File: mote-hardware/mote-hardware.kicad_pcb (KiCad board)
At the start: 2 copper layers, 52 x 51 mm, 43 parts, among them J1 USB_B_Micro, J2 Conn_02x18_Odd_Even, J3 Conn_02x18_Odd_Even, J4 SM03B-SRSS-TB, SW1 SW_Push, SW2 SW_Push, U1 RP2350_60QFN, U2 NCP1117-3.3_SOT223, U3 W25Q128JVS, Y1 ABM8-272-T3

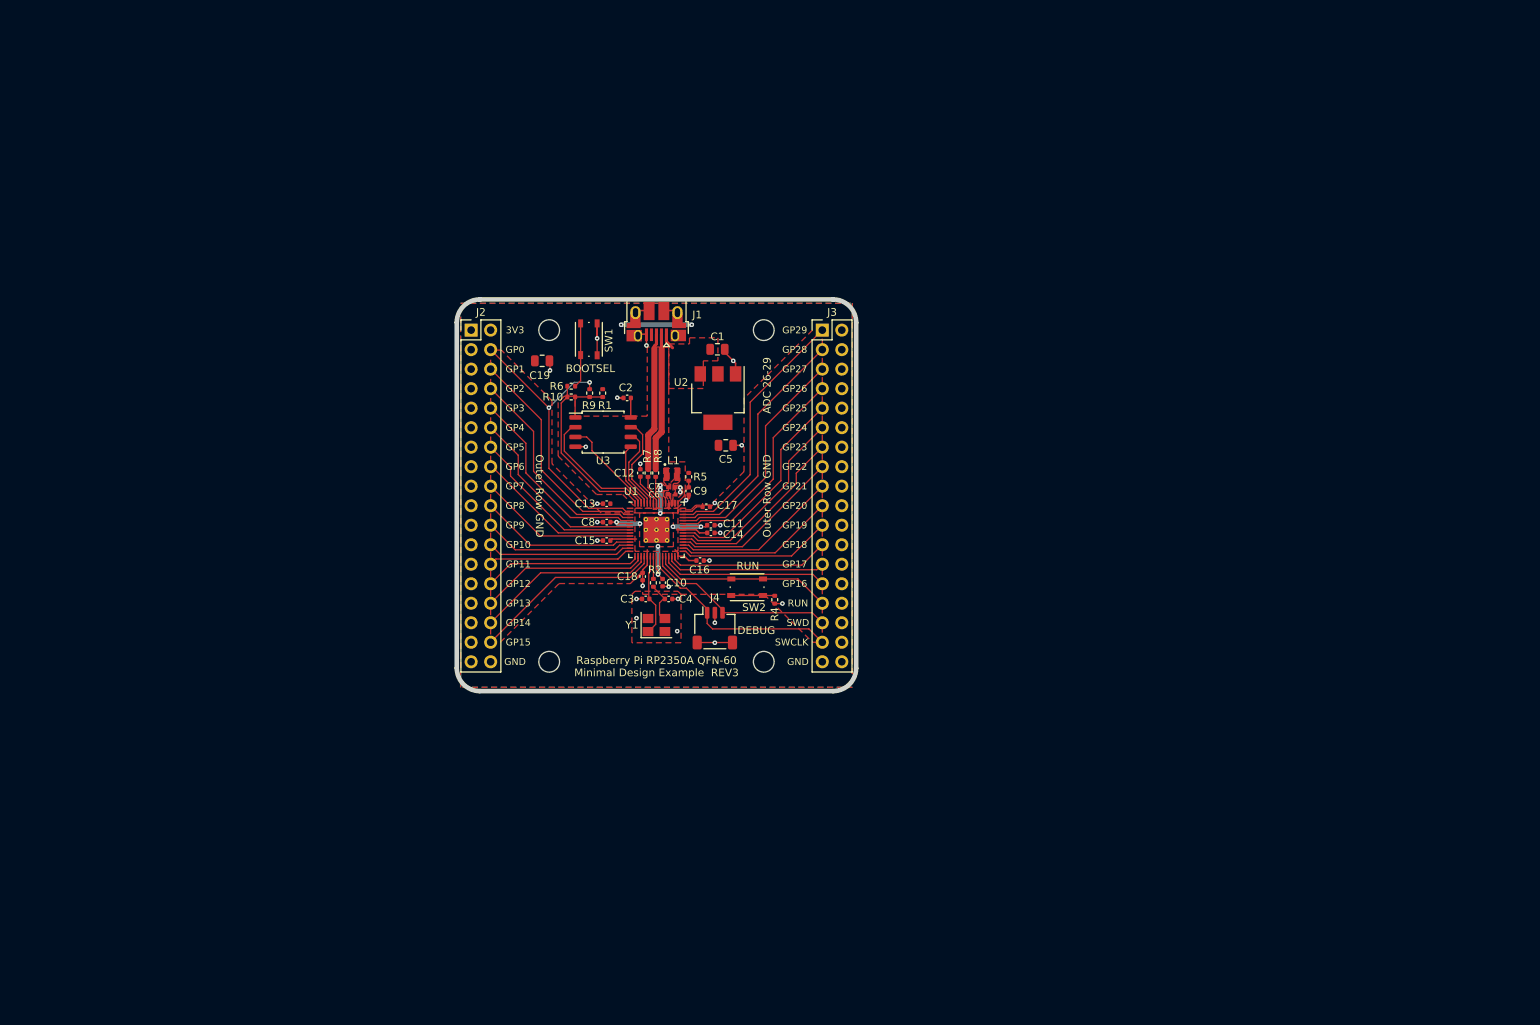
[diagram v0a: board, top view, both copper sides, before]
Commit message: Start of PCB layout
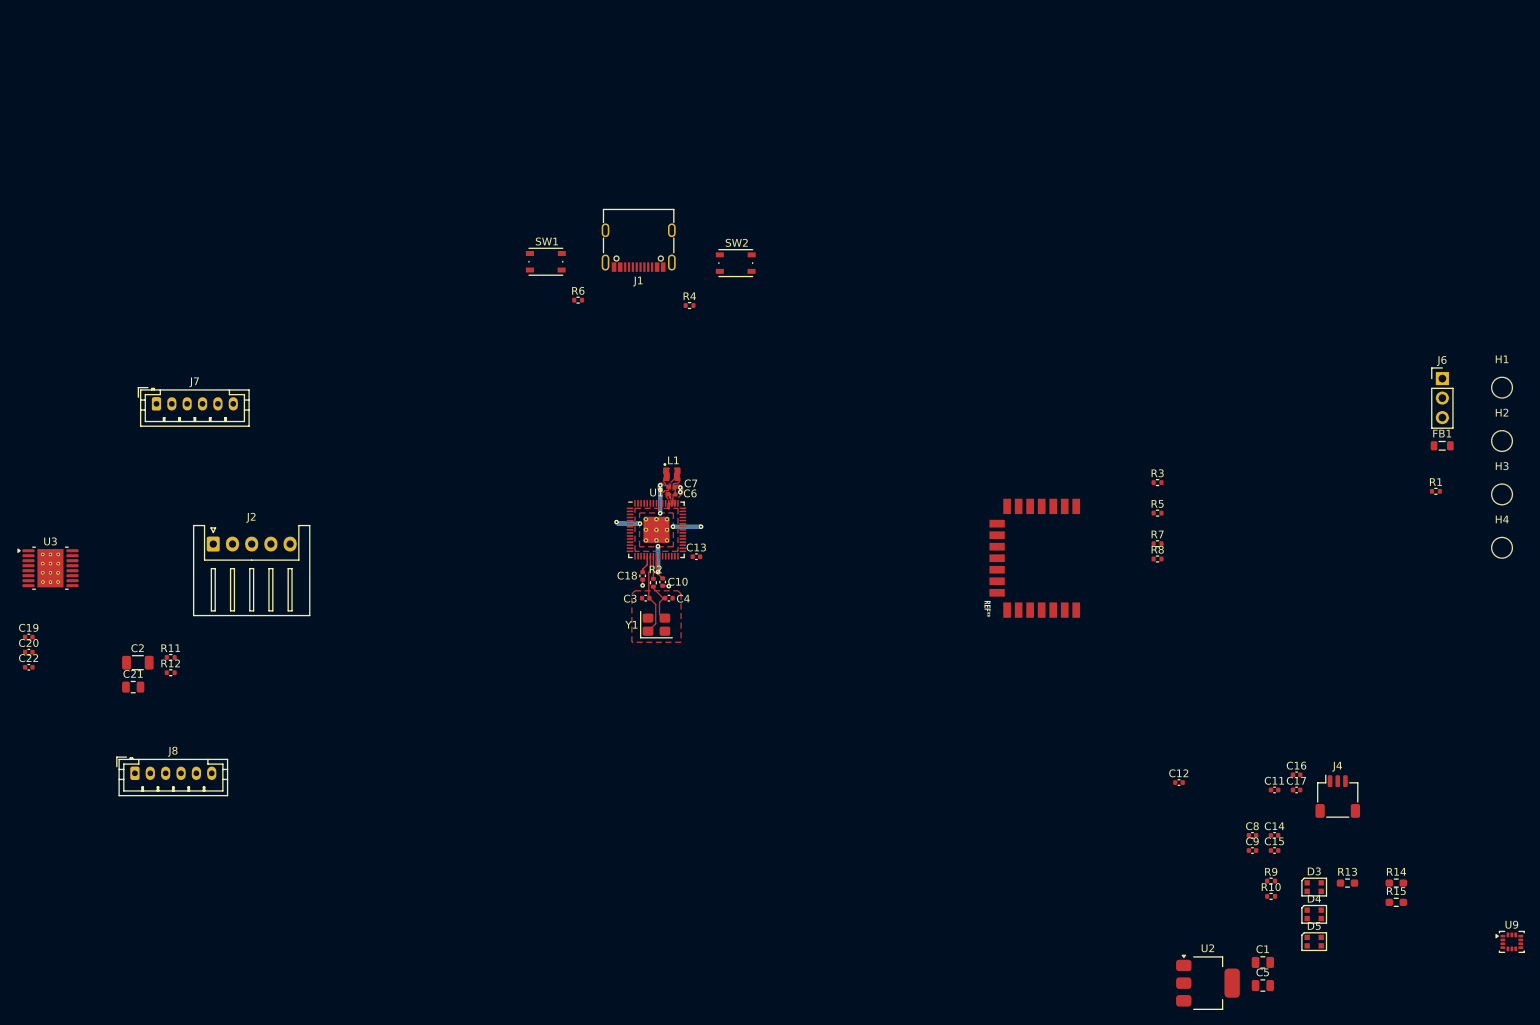
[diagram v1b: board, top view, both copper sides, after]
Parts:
- removed J3: Conn_02x18_Odd_Even, Connector_PinHeader_2.54mm:PinHeader_2x18_P2.54mm_Vertical
- added C20: 2.2u, Capacitor_SMD:C_0402_1005Metric, F.Cu at (18.3, 115.9)
- added C21: 10uF, Capacitor_SMD:C_0805_2012Metric, F.Cu at (31.9, 120.5)
- added C22: 0.1uF, Capacitor_SMD:C_0402_1005Metric, F.Cu at (18.3, 117.9)
- added D3: WS2812B-2020, LED_SMD:LED_WS2812B-2020_PLCC4_2.0x2.0mm, F.Cu at (185.6, 146.5)
- added D4: WS2812B-2020, LED_SMD:LED_WS2812B-2020_PLCC4_2.0x2.0mm, F.Cu at (185.6, 150.1)
- added D5: WS2812B-2020, LED_SMD:LED_WS2812B-2020_PLCC4_2.0x2.0mm, F.Cu at (185.6, 153.6)
- added FB1: 300, Inductor_SMD:L_0805_2012Metric, F.Cu at (202.3, 89.1)
- added J6: Conn_01x03_Pin, Connector_PinHeader_2.54mm:PinHeader_1x03_P2.54mm_Vertical, F.Cu at (202.3, 80.3)
- added J7: left_motor, Connector_JST:JST_PH_B6B-PH-K_1x06_P2.00mm_Vertical, F.Cu at (34.9, 83.6)
- added J8: right_motor, Connector_JST:JST_PH_B6B-PH-K_1x06_P2.00mm_Vertical, F.Cu at (32.1, 131.7)
- added R11: 200m, Resistor_SMD:R_0402_1005Metric, F.Cu at (36.8, 116.6)
- added R12: 200m, Resistor_SMD:R_0402_1005Metric, F.Cu at (36.8, 118.6)
- added R13: 560, Resistor_SMD:R_0603_1608Metric_Pad0.98x0.95mm_HandSolder, F.Cu at (190.0, 146.0)
- added R14: 10k, Resistor_SMD:R_0603_1608Metric_Pad0.98x0.95mm_HandSolder, F.Cu at (196.3, 146.0)
- added R15: 10k, Resistor_SMD:R_0603_1608Metric_Pad0.98x0.95mm_HandSolder, F.Cu at (196.3, 148.5)
- added R3: 10k, Resistor_SMD:R_0402_1005Metric, F.Cu at (165.2, 93.8)
- added U4: RP Radio Module 2, mote-hardware:rpi_rmc20452t, F.Cu at (152.1, 103.7)
- added U9: LSM6DS3, Package_LGA:LGA-14_3x2.5mm_P0.5mm_LayoutBorder3x4y, F.Cu at (211.4, 153.7)
- C19: value 10u -> 0.01u; footprint Capacitor_SMD:C_0805_2012Metric -> Capacitor_SMD:C_0402_1005Metric
- C2: value 100n -> 100uF; footprint Capacitor_SMD:C_0402_1005Metric -> Capacitor_SMD:C_1206_3216Metric
- H1, H2, H3, H4: value MountingHole -> M2.5 loose
- J1: value USB_B_Micro -> USB_C_Receptacle_USB2.0_14P; footprint Connector_USB:USB_Micro-B_Amphenol_10103594-0001LF_Horizontal -> Connector_USB:USB_C_Receptacle_G-Switch_GT-USB-7010ASV
- J2: value Conn_02x18_Odd_Even -> JST_XH2.54-SP; footprint Connector_PinHeader_2.54mm:PinHeader_2x18_P2.54mm_Vertical -> Connector_JST:JST_XH_S5B-XH-A_1x05_P2.50mm_Horizontal
- R1: value DNF -> 470
- R10: value 0 -> 5.1k
- R9: value DNF -> 5.1k
- U3: value W25Q128JVS -> DRV8833PWP; footprint Package_SO:SOIC-8_5.23x5.23mm_P1.27mm -> Package_SO:HTSSOP-16-1EP_4.4x5mm_P0.65mm_EP3.4x5mm_Mask2.46x2.31mm_ThermalVias
- moved H4 124.9 mm to (210.1, 102.3)
- moved H1 124.3 mm to (210.1, 81.5)
- moved R10 111.9 mm to (180.0, 147.7)
- moved R1 109.2 mm to (201.5, 95.0), turned to 0 degrees
- moved R9 109.1 mm to (180.0, 145.7), turned to 0 degrees
- moved C1 106.8 mm to (178.9, 156.3)
- moved U2 99.4 mm to (171.8, 159.0), turned to 0 degrees
- moved C5 99.2 mm to (178.9, 159.3)
- moved H3 98.6 mm to (210.1, 95.4)
- moved H2 97.2 mm to (210.1, 88.4)
- moved C15 95.9 mm to (180.5, 141.8), turned to 0 degrees
- moved C8 93.4 mm to (177.6, 139.8), turned to 0 degrees
- moved C9 87.1 mm to (177.6, 141.8), turned to 0 degrees
- moved C17 85.2 mm to (183.3, 133.9)
- moved J4 84.0 mm to (188.7, 134.7)
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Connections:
- net +1V1 renamed /rp2354/+1v1
- net /RUN renamed /rp2354/RUN
- net /SWCLK renamed /rp2354/SWCLK
- net /SWD renamed /rp2354/SWD
- net /VREG_AVDD renamed /rp2354/VREG_AVDD
- net /VREG_LX renamed /rp2354/VREG_LX
- net /XIN renamed /rp2354/XIN
- net /XOUT renamed /rp2354/XOUT
- net /~{USB_BOOT} renamed /rp2354/~{USB_BOOT}
- C1 pad 1: VBUS -> /+5v
- C12 pad 1: +3V3 -> /+3v3
- C13 pad 1: +3V3 -> /+3v3
- C14 pad 1: +3V3 -> /+3v3
- C15 pad 1: +3V3 -> /+3v3
- C16 pad 1: +3V3 -> /+3v3
- C17 pad 1: +3V3 -> /+3v3
- C18 pad 1: +3V3 -> /+3v3
- C19 pad 1: +3V3 -> Net-(U3-VCP)
- C19 pad 2: GND -> /+5v
- C2 pad 1: +3V3 -> /+5v
- C5 pad 1: +3V3 -> /+3v3
- C6 pad 1: +3V3 -> /+3v3
- J2 pad 1: GND -> /+5v
- J2 pad 2: +3V3 -> /lidar_rx
- J2 pad 3: GND -> /lidar_tx
- J2 pad 4: /GPIO0 -> GND
- J2 pad 5: GND -> unconnected-(J2-Pin_5-Pad5)
- R1 pad 1: +3V3 -> /rp2354/GPIO24
- R1 pad 2: /FLASH_SS -> Net-(U4-DO)
- R10 pad 1: /QSPI_SS -> /CC2
- R10 pad 2: /FLASH_SS -> GND
- R5 pad 1: +3V3 -> /+3v3
- R6 pad 1: /QSPI_SS -> /rp2354/QSPI_SS
- R9 pad 1: /GPIO0 -> /CC1
- R9 pad 2: /FLASH_SS -> GND
- U1 pad 1: +3V3 -> /+3v3
- U1 pad 10: /GPIO7 -> /motor_left_encoder_b
- U1 pad 11: +3V3 -> /+3v3
- U1 pad 12: /GPIO8 -> /motor_right_encoder_a
- U1 pad 13: /GPIO9 -> /motor_right_encoder_b
- U1 pad 14: /GPIO10 -> /motor_left_input_a
- U1 pad 15: /GPIO11 -> /motor_left_input_b
- U1 pad 16: /GPIO12 -> /motor_right_input_a
- U1 pad 17: /GPIO13 -> /motor_right_input_b
- U1 pad 18: /GPIO14 -> /imu_sda
- U1 pad 19: /GPIO15 -> /imu_scl
- U1 pad 2: /GPIO0 -> /rp2354/GPIO0
- U1 pad 20: +3V3 -> /+3v3
- U1 pad 27: /GPIO16 -> /rp2354/GPIO16
- U1 pad 28: /GPIO17 -> /rp2354/GPIO17
- U1 pad 29: /GPIO18 -> /motor_standby
- U1 pad 3: /GPIO1 -> /rp2354/GPIO1
- U1 pad 30: +3V3 -> /+3v3
- U1 pad 31: /GPIO19 -> /status_led_tx
- U1 pad 32: /GPIO20 -> /rp2354/GPIO20
- U1 pad 33: /GPIO21 -> /rp2354/GPIO21
- U1 pad 34: /GPIO22 -> /rp2354/GPIO22
- U1 pad 35: /GPIO23 -> /rp2354/GPIO23
- U1 pad 36: /GPIO24 -> /rp2354/GPIO24
- U1 pad 37: /GPIO25 -> /rp2354/GPIO25
- U1 pad 38: +3V3 -> /+3v3
- U1 pad 4: /GPIO2 -> /rp2354/GPIO2
- U1 pad 40: /GPIO26_ADC0 -> /CC1
- U1 pad 41: /GPIO27_ADC1 -> /CC2
- U1 pad 42: /GPIO28_ADC2 -> /rp2354/GPIO28_ADC2
- U1 pad 43: /GPIO29_ADC3 -> /rp2354/GPIO29_ADC3
- U1 pad 44: +3V3 -> /+3v3
- U1 pad 45: +3V3 -> /+3v3
- U1 pad 49: +3V3 -> /+3v3
- U1 pad 5: /GPIO3 -> /rp2354/GPIO3
- U1 pad 53: +3V3 -> /+3v3
- U1 pad 54: +3V3 -> /+3v3
- U1 pad 55: /QSPI_SD3 -> /rp2354/QSPI_SD3
- U1 pad 56: /QSPI_SCLK -> /rp2354/QSPI_SCLK
- U1 pad 57: /QSPI_SD0 -> /rp2354/QSPI_SD0
- U1 pad 58: /QSPI_SD2 -> /rp2354/QSPI_SD2
- U1 pad 59: /QSPI_SD1 -> /rp2354/QSPI_SD1
- U1 pad 60: /QSPI_SS -> /rp2354/QSPI_SS
- U1 pad 7: /GPIO4 -> /lidar_tx
- U1 pad 8: /GPIO5 -> /lidar_rx
- U1 pad 9: /GPIO6 -> /motor_left_encoder_a
- U2 pad 2: +3V3 -> /+3v3
- U2 pad 3: VBUS -> /+5v
- U3 pad 1: /FLASH_SS -> /motor_standby
- U3 pad 2: /QSPI_SD1 -> Net-(J7-Pin_5)
- U3 pad 3: /QSPI_SD2 -> Net-(U3-AISEN)
- U3 pad 4: GND -> Net-(J7-Pin_6)
- U3 pad 5: /QSPI_SD0 -> Net-(J8-Pin_6)
- U3 pad 6: /QSPI_SCLK -> Net-(U3-BISEN)
- U3 pad 7: /QSPI_SD3 -> Net-(J8-Pin_5)
- U3 pad 8: +3V3 -> unconnected-(U3-~{FAULT}-Pad8)
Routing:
- net /GPIO0: track 39.0 -> 0.00 mm, vias 2 -> 0
- net +3V3: track 37.6 -> 0.00 mm, vias 2 -> 0
- net GND: track 37.5 -> 1.58 mm, vias 27 -> 4
- net /GPIO29_ADC3: track 33.6 -> 0.00 mm
- net /GPIO28_ADC2: track 31.9 -> 0.00 mm
- net /GPIO27_ADC1: track 30.3 -> 0.00 mm
- net /GPIO1: track 29.8 -> 0.00 mm
- net /GPIO26_ADC0: track 28.6 -> 0.00 mm
- net /GPIO2: track 28.2 -> 0.00 mm
- net /rp2354/SWCLK: track 27.8 -> 0.00 mm
- net /GPIO25: track 27.7 -> 0.00 mm
- net /GPIO3: track 26.5 -> 0.00 mm
- net /GPIO24: track 26.1 -> 0.00 mm
- net /rp2354/SWD: track 25.4 -> 0.00 mm
- net /GPIO15: track 25.2 -> 0.00 mm
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- added copper zone on F.Cu, net +1V1
- added copper zone on F.Cu, net /VREG_LX
- removed copper zone on F.Cu, net /rp2354/+1v1
- removed copper zone on F.Cu, net /rp2354/VREG_LX
- removed copper zone on B.Cu, net GND
- removed copper zone on F.Cu, net VBUS
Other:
- board outline removed
- board text removed: "3V3"
- board text removed: "ADC 26-29"
- board text removed: "BOOTSEL"
- board text removed: "DEBUG"
- board text removed: "GND"
- board text removed: "GP0"
- board text removed: "GP1"
- board text removed: "GP10"
- board text removed: "GP11"
- board text removed: "GP12"
- board text removed: "GP13"
- board text removed: "GP14"
- board text removed: "GP15"
- board text removed: "GP16"
- board text removed: "GP17"
- board text removed: "GP18"
- board text removed: "GP19"
- board text removed: "GP2"
- board text removed: "GP20"
- board text removed: "GP21"
- board text removed: "GP22"
- board text removed: "GP23"
- board text removed: "GP24"
- board text removed: "GP25"
- board text removed: "GP26"
- board text removed: "GP27"
- board text removed: "GP28"
- board text removed: "GP29"
- board text removed: "GP3"
- board text removed: "GP4"
- board text removed: "GP5"
- board text removed: "GP6"
- board text removed: "GP7"
- board text removed: "GP8"
- board text removed: "GP9"
- board text removed: "Minimal Design Example REV3"
- board text removed: "Outer Row GND"
- board text removed: "RUN"
- board text removed: "Raspberry Pi RP2350A QFN-60"
- board text removed: "SWCLK"
- board text removed: "SWD"

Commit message: Get pcb ready for first prototype order
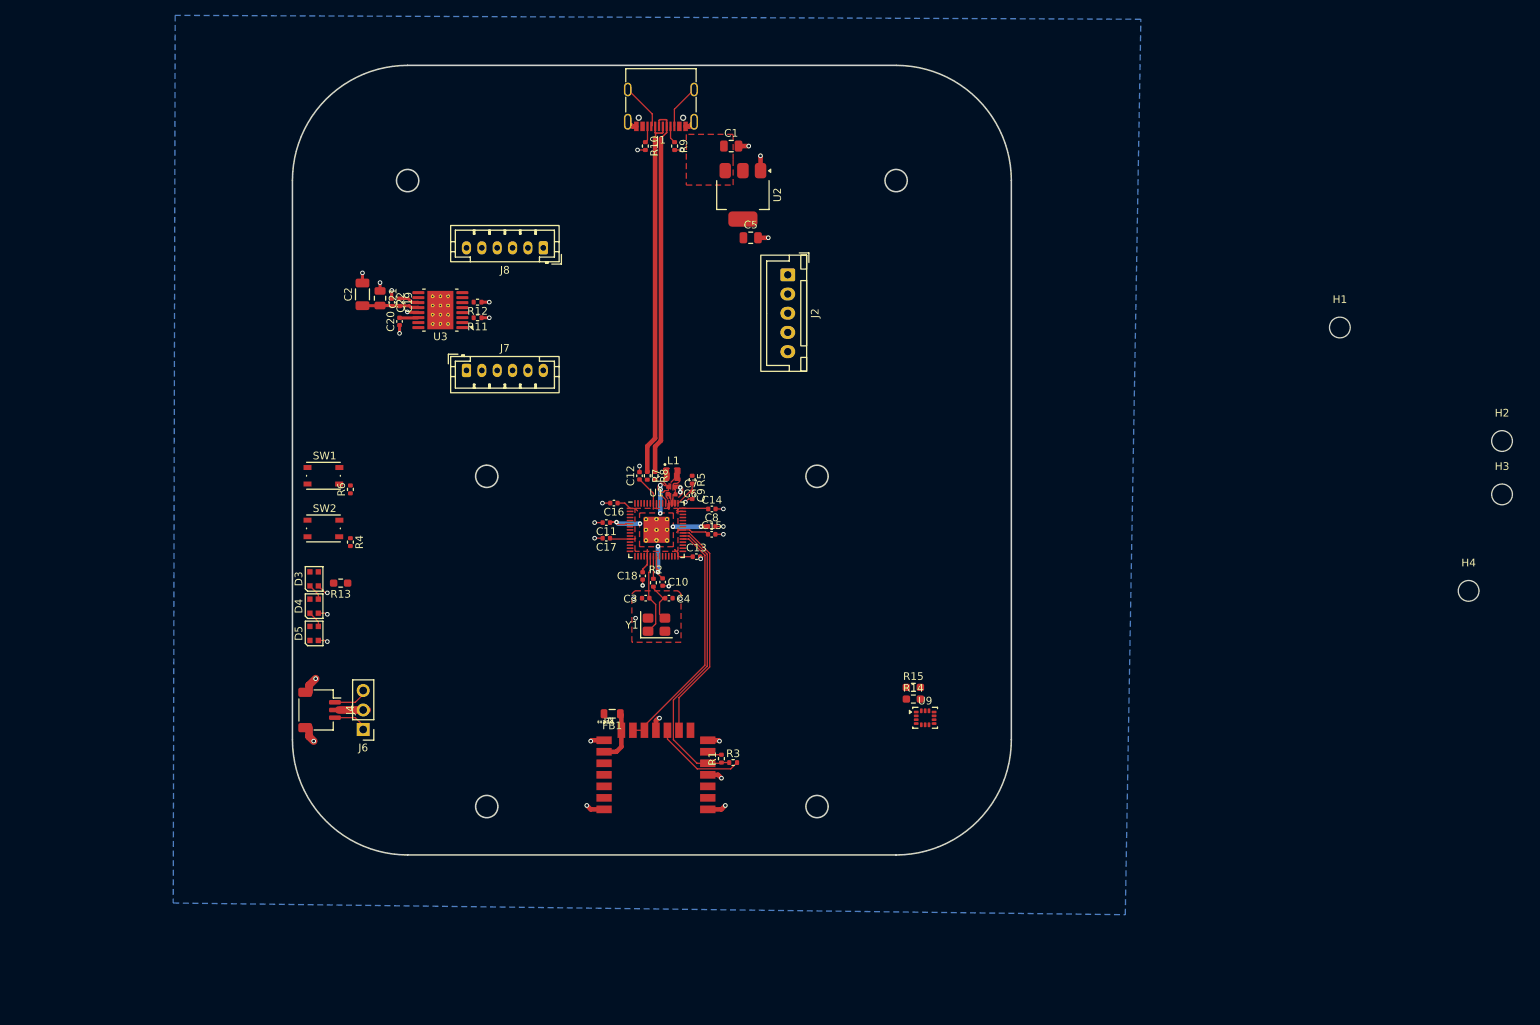
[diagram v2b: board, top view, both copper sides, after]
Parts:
- J2: footprint Connector_JST:JST_XH_S5B-XH-A_1x05_P2.50mm_Horizontal -> Connector_JST:JST_XH_B5B-XH-A_1x05_P2.50mm_Vertical
- moved J6 147.7 mm to (61.8, 126.0), turned to 180 degrees
- moved R13 136.8 mm to (58.9, 106.9), turned to 180 degrees
- moved D4 136.3 mm to (55.4, 109.9), turned to 90 degrees
- moved D5 136.3 mm to (55.4, 113.5), turned to 90 degrees
- moved D3 136.3 mm to (55.4, 106.4), turned to 90 degrees
- moved J4 133.0 mm to (56.1, 123.5), turned to -90 degrees
- moved R10 127.2 mm to (98.6, 50.0), turned to -90 degrees
- moved C1 126.8 mm to (109.7, 50.0)
- moved R9 123.2 mm to (102.4, 50.0), turned to -90 degrees
- moved U2 119.2 mm to (111.3, 56.4), turned to -90 degrees
- moved C5 118.0 mm to (112.3, 62.0)
- moved FB1 113.6 mm to (94.2, 124.0), turned to 180 degrees
- moved R1 99.3 mm to (108.5, 129.8), turned to 90 degrees
- moved C16 95.7 mm to (94.5, 96.5), turned to 180 degrees
- moved C17 95.7 mm to (93.5, 101.1), turned to 180 degrees
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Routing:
- net GND: track 1.58 -> 63.2 mm, vias 4 -> 40
- net /USB_D-: track 0.00 -> 48.3 mm
- net /USB_D+: track 0.00 -> 47.2 mm
- net /rp2354/GPIO24: track 0.00 -> 38.7 mm
- net /rp2354/GPIO23: track 0.00 -> 31.3 mm
- net /rp2354/GPIO25: track 0.00 -> 29.3 mm
- net /+3v3: track 2.39 -> 28.4 mm
- net /rp2354/+1v1: track 6.58 -> 23.3 mm, vias 2 -> 9
- net Net-(U4-nIRQ): track 0.00 -> 12.2 mm
- net +1V1: track 10.1 -> 0.00 mm, vias 7 -> 0
- net /+5v: track 0.00 -> 7.42 mm
- net Net-(U4-VDDIO): track 0.00 -> 6.87 mm
- net /rp2354/SWD: track 0.00 -> 4.32 mm
- net /rp2354/SWCLK: track 0.00 -> 4.32 mm
- net /rp2354/VREG_AVDD: track 0.00 -> 3.53 mm
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- added copper zone on F.Cu, net (none)
- added copper zone on F.Cu, net /+3v3
- added copper zone on F.Cu, net /+5v
- added copper zone on F.Cu, net /rp2354/+1v1
- added copper zone on F.Cu, net /rp2354/VREG_LX
- added copper zone on B.Cu, net GND
- removed copper zone on F.Cu, net +1V1
- removed copper zone on F.Cu, net +3V3
- removed copper zone on F.Cu, net /VREG_LX
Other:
- board outline added: 93.6 x 102.8 mm

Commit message: Routing
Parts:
- moved U9 37.2 mm to (99.5, 113.5)
- moved R14 36.8 mm to (98.6, 110.2), turned to -90 degrees
- moved R15 34.9 mm to (100.1, 110.2), turned to -90 degrees
- moved J2 25.2 mm to (91.9, 65.9)
- moved J8 14.1 mm to (71.2, 63.2), turned to 0 degrees
- moved C3 6.93 mm to (98.7, 102.0)
- moved C4 6.93 mm to (101.7, 102.0)
- moved C6 6.93 mm to (102.1, 88.5)
- moved C7 6.93 mm to (102.1, 87.5)
- moved C9 6.93 mm to (104.7, 88.6)
- moved C10 6.93 mm to (100.9, 99.9)
- moved C11 6.93 mm to (93.5, 92.1)
- moved C12 6.93 mm to (97.9, 86.0)
- moved C13 6.93 mm to (105.3, 96.6)
- moved C14 6.93 mm to (107.3, 90.4)
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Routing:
- net /rp2354/SWD: track 4.32 -> 73.6 mm
- net /rp2354/SWCLK: track 4.32 -> 71.2 mm
- net /imu_scl: track 0.00 -> 19.3 mm
- net /imu_sda: track 0.00 -> 18.0 mm
- net Net-(J7-Pin_6): track 0.00 -> 15.9 mm
- net Net-(J8-Pin_6): track 0.00 -> 14.4 mm
- net Net-(J8-Pin_5): track 0.00 -> 12.4 mm
- net Net-(J7-Pin_5): track 0.00 -> 7.69 mm
- net /rp2354/GPIO25: track 29.3 -> 36.3 mm
- net /rp2354/GPIO24: track 38.7 -> 45.7 mm
- net /rp2354/GPIO23: track 31.3 -> 38.3 mm
- net /USB_D+: track 47.2 -> 40.3 mm
- net /USB_D-: track 48.3 -> 41.4 mm
- net /rp2354/~{USB_BOOT}: track 0.00 -> 5.66 mm
- net Net-(R4-Pad1): track 0.00 -> 4.15 mm
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
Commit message: Finish routing
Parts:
- removed U3: DRV8833PWP, Package_SO:HTSSOP-16-1EP_4.4x5mm_P0.65mm_EP3.4x5mm_Mask2.46x2.31mm_ThermalVias
- added U5: DRV8833PW, Package_SO:TSSOP-16-1EP_4.4x5mm_P0.65mm, F.Cu at (80.2, 71.2)
- J4: footprint Connector_JST:JST_SH_SM03B-SRSS-TB_1x03-1MP_P1.00mm_Horizontal -> Connector_JST:JST_SH_BM03B-SRSS-TB_1x03-1MP_P1.00mm_Vertical
- U1: value RP2350_60QFN -> RP2354_60QFN
- moved H4 130.9 mm to (77.9, 136.1)
- moved H1 112.8 mm to (77.9, 93.0)
- moved H3 98.0 mm to (120.9, 136.0)
- moved H2 89.3 mm to (120.9, 93.0)
- moved C2 12.5 mm to (70.1, 69.2)
- moved C21 12.5 mm to (72.4, 69.7)
- moved C22 12.5 mm to (73.9, 70.2)
- moved R11 12.5 mm to (86.4, 73.2)
- moved R12 12.5 mm to (86.4, 69.4)
- moved C19 12.5 mm to (74.9, 70.2)
- moved C20 12.5 mm to (74.9, 72.7)
- moved J4 7.56 mm to (63.2, 120.9)
- moved J6 7.56 mm to (68.9, 123.4)
- moved D3 6.42 mm to (61.8, 106.1)
- moved D4 6.42 mm to (61.8, 109.6)
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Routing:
- net /motor_standby: track 0.00 -> 104.8 mm, vias 0 -> 4
- net /rp2354/RUN: track 4.12 -> 73.2 mm
- net /status_led_tx: track 0.00 -> 68.8 mm
- net /+3v3: track 28.4 -> 85.4 mm, vias 0 -> 7
- net /motor_right_input_b: track 0.00 -> 52.5 mm, vias 0 -> 2
- net /CC2: track 2.17 -> 54.5 mm, vias 0 -> 2
- net /motor_right_encoder_a: track 0.00 -> 51.2 mm
- net /CC1: track 2.28 -> 52.4 mm
- net /motor_right_encoder_b: track 0.00 -> 50.0 mm
- net /motor_right_input_a: track 0.00 -> 48.8 mm, vias 0 -> 2
- net /motor_left_input_b: track 0.00 -> 40.8 mm
- net /motor_left_input_a: track 0.00 -> 39.2 mm
- net /rp2354/QSPI_SS: track 0.00 -> 36.3 mm, vias 0 -> 2
- net /+5v: track 11.0 -> 41.6 mm, vias 0 -> 2
- net /lidar_rx: track 0.00 -> 29.5 mm
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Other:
- outline, holes or cut-outs redrawn
